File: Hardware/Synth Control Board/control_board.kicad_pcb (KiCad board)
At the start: 2 copper layers, 149.9 x 147.3 mm, 55 parts, among them J1 Conn_01x13, J10 Conn_01x05, J11 Conn_01x08, J2 Conn_01x03, J3 Conn_01x13, J4 Conn_01x13, J5 Conn_01x08, J6 Conn_01x13, J7 Conn_01x05, J8 Conn_01x05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

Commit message: redo control board layout. Initial version, might need more work.
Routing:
- net +5V: track 0.00 -> 1180.4 mm
- net /osc3_freq_wiper: track 0.00 -> 143.7 mm
- net /osc2_freq_wiper: track 0.00 -> 137.7 mm
- net /osc4_freq_wiper: track 0.00 -> 134.1 mm
- net /osc1_freq_wiper: track 0.00 -> 130.1 mm
- net /osc3_pwm_wiper: track 0.00 -> 123.3 mm
- net /osc4_pwm_wiper: track 0.00 -> 113.1 mm
- net /osc1_pwm_wiper: track 0.00 -> 112.9 mm
- net /osc2_pwm_wiper: track 0.00 -> 110.3 mm
- net /vol_out_1: track 0.00 -> 94.3 mm
- net /vol_in_1: track 0.00 -> 91.7 mm
- net /delay_out_1: track 0.00 -> 77.4 mm
- net /delay_in_1: track 0.00 -> 72.0 mm
- net /delay_out_2: track 0.00 -> 60.7 mm
- net /vol_out_4: track 0.00 -> 57.5 mm
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- added copper zone on B.Cu, net GND
- added copper zone on F.Cu, net GND

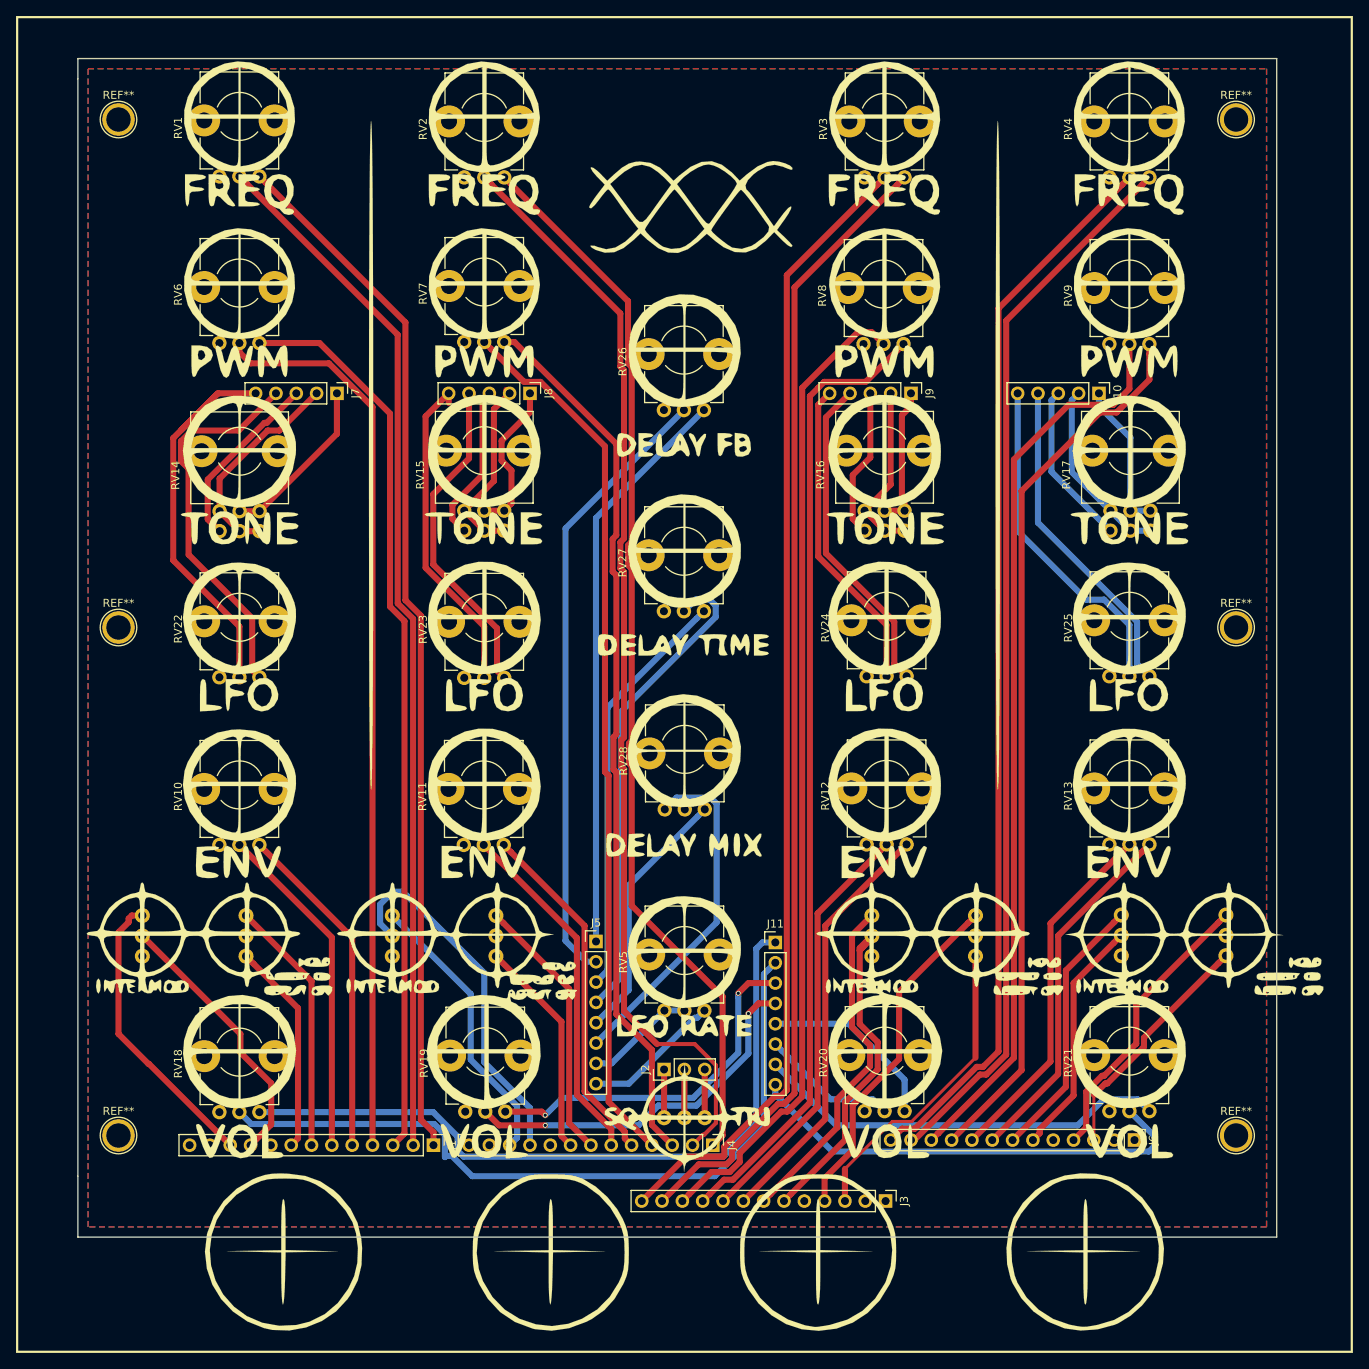
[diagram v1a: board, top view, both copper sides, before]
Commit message: add quantization again, fix connectors again, add mounting holes to main board
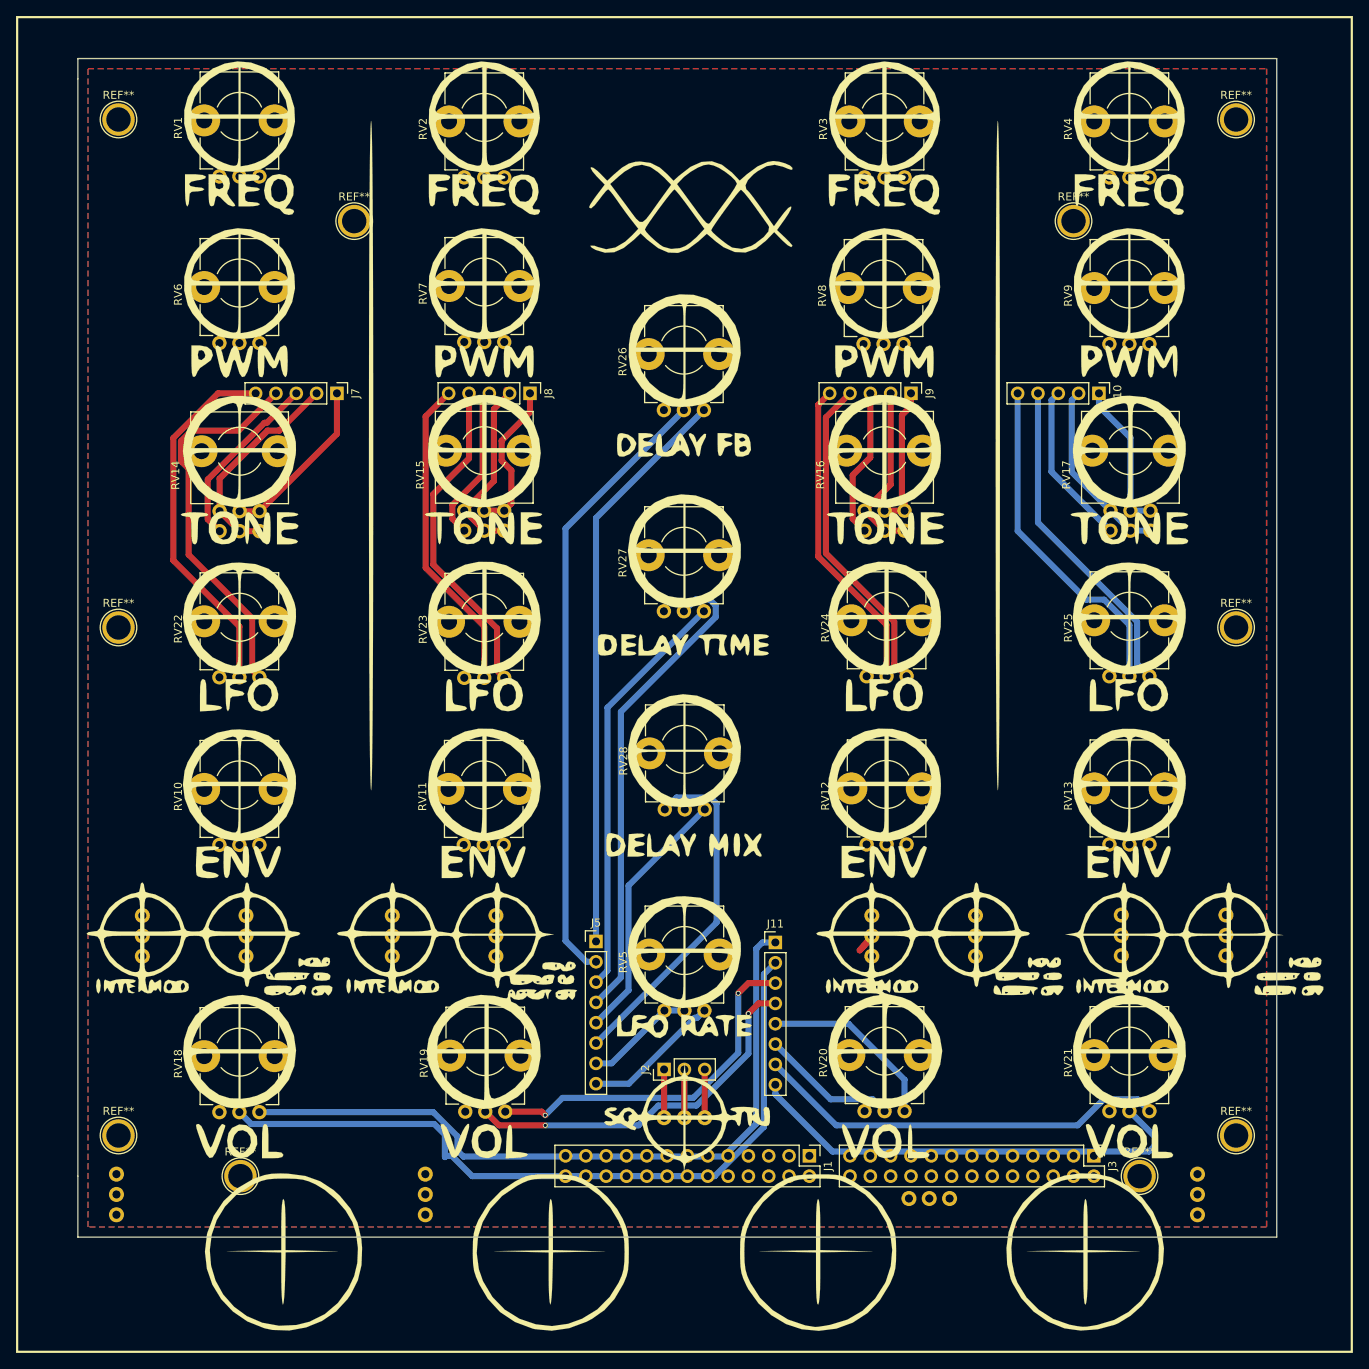
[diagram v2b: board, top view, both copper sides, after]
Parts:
- removed J4, J6: Conn_01x13, Pin_Headers:Pin_Header_Straight_1x13_Pitch2.54mm
- added REF**: 1pin, Connectors:1pin, F.Cu at (42.2, 25.4)
- added REF**: 1pin, Connectors:1pin, F.Cu at (132.1, 25.4)
- added REF**: 1pin, Connectors:1pin, F.Cu at (140.3, 144.8)
- added REF**: 1pin, Connectors:1pin, F.Cu at (27.9, 144.8)
- added SW10: SW_SPST, SparkFun-Electromechanical:SWITCH-SPDT, F.Cu at (28.6, 114.7)
- added SW11: SW_SPST, SparkFun-Electromechanical:SWITCH-SPDT, F.Cu at (59.9, 114.7)
- added SW12: SW_SPST, SparkFun-Electromechanical:SWITCH-SPDT, F.Cu at (119.8, 114.7)
- added SW13: SW_SPST, SparkFun-Electromechanical:SWITCH-SPDT, F.Cu at (151.1, 114.7)
- J1, J3: value Conn_01x13 -> Conn_02x13_Odd_Even; footprint Pin_Headers:Pin_Header_Straight_1x13_Pitch2.54mm -> Pin_Headers:Pin_Header_Straight_2x13_Pitch2.54mm
- moved J1 47.0 mm to (99.1, 142.2)
- moved SW9 36.2 mm to (12.4, 147.1)
- moved SW8 33.5 mm to (51.1, 147.1)
- moved SW7 33.3 mm to (114.0, 147.6), turned to 90 degrees
- moved SW6 32.6 mm to (147.6, 147.1)
- moved J3 26.6 mm to (134.6, 142.2)
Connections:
- J1 pad 10: /envelope_pwm_bypass_out_1 -> +5V
- J1 pad 11: /envelope_pwm_bypass_in_1 -> /osc1_speed
- J1 pad 12: GND -> /osc2_speed
- J1 pad 13: GND -> /osc1_hold
- J1 pad 2: /osc1_freq_wiper -> +5V
- J1 pad 3: +5V -> /osc1_freq_wiper
- J1 pad 4: /osc1_pwm_wiper -> /osc2_freq_wiper
- J1 pad 6: /osc1_speed -> +5V
- J1 pad 7: /osc1_hold -> /osc1_pwm_wiper
- J1 pad 8: /osc1_repeat -> /osc2_pwm_wiper
- J1 pad 9: /osc1_quant -> +5V
- J3 pad 10: +5V -> /osc4_quant
- J3 pad 11: /osc3_pwm_wiper -> /envelope_pwm_bypass_out_3
- J3 pad 12: +5V -> /envelope_pwm_bypass_out_4
- J3 pad 13: /osc3_freq_wiper -> /envelope_pwm_bypass_in_3
- J3 pad 3: /osc3_repeat -> GND
- J3 pad 4: /osc3_hold -> GND
- J3 pad 5: /osc3_quant -> /osc3_repeat
- J3 pad 6: /envelope_pwm_bypass_out_3 -> /osc4_repeat
- J3 pad 7: /envelope_pwm_bypass_in_3 -> /osc3_hold
- J3 pad 8: +5V -> /osc4_hold
- J3 pad 9: /osc3_speed -> /osc3_quant
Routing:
- net +5V: track 1180.4 -> 0.00 mm
- net /osc3_freq_wiper: track 143.7 -> 0.00 mm
- net /osc2_freq_wiper: track 137.7 -> 0.00 mm
- net /osc4_freq_wiper: track 134.1 -> 0.00 mm
- net /osc1_freq_wiper: track 130.1 -> 0.00 mm
- net /osc3_pwm_wiper: track 123.3 -> 0.00 mm
- net /osc4_pwm_wiper: track 113.1 -> 0.00 mm
- net /osc1_pwm_wiper: track 112.9 -> 0.00 mm
- net /osc2_pwm_wiper: track 110.3 -> 0.00 mm
- net /osc3_speed: track 53.0 -> 0.00 mm
- net /envelope_pwm_bypass_out_2: track 46.3 -> 0.00 mm
- net /osc4_speed: track 45.1 -> 0.00 mm
- net /osc2_speed: track 44.1 -> 0.00 mm
- net /osc3_hold: track 43.5 -> 0.00 mm
- net /envelope_pwm_bypass_in_3: track 43.2 -> 0.00 mm
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
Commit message: reroute connector board with 2-row connectors. Hold switch placement is temporary. Need to find room for this.
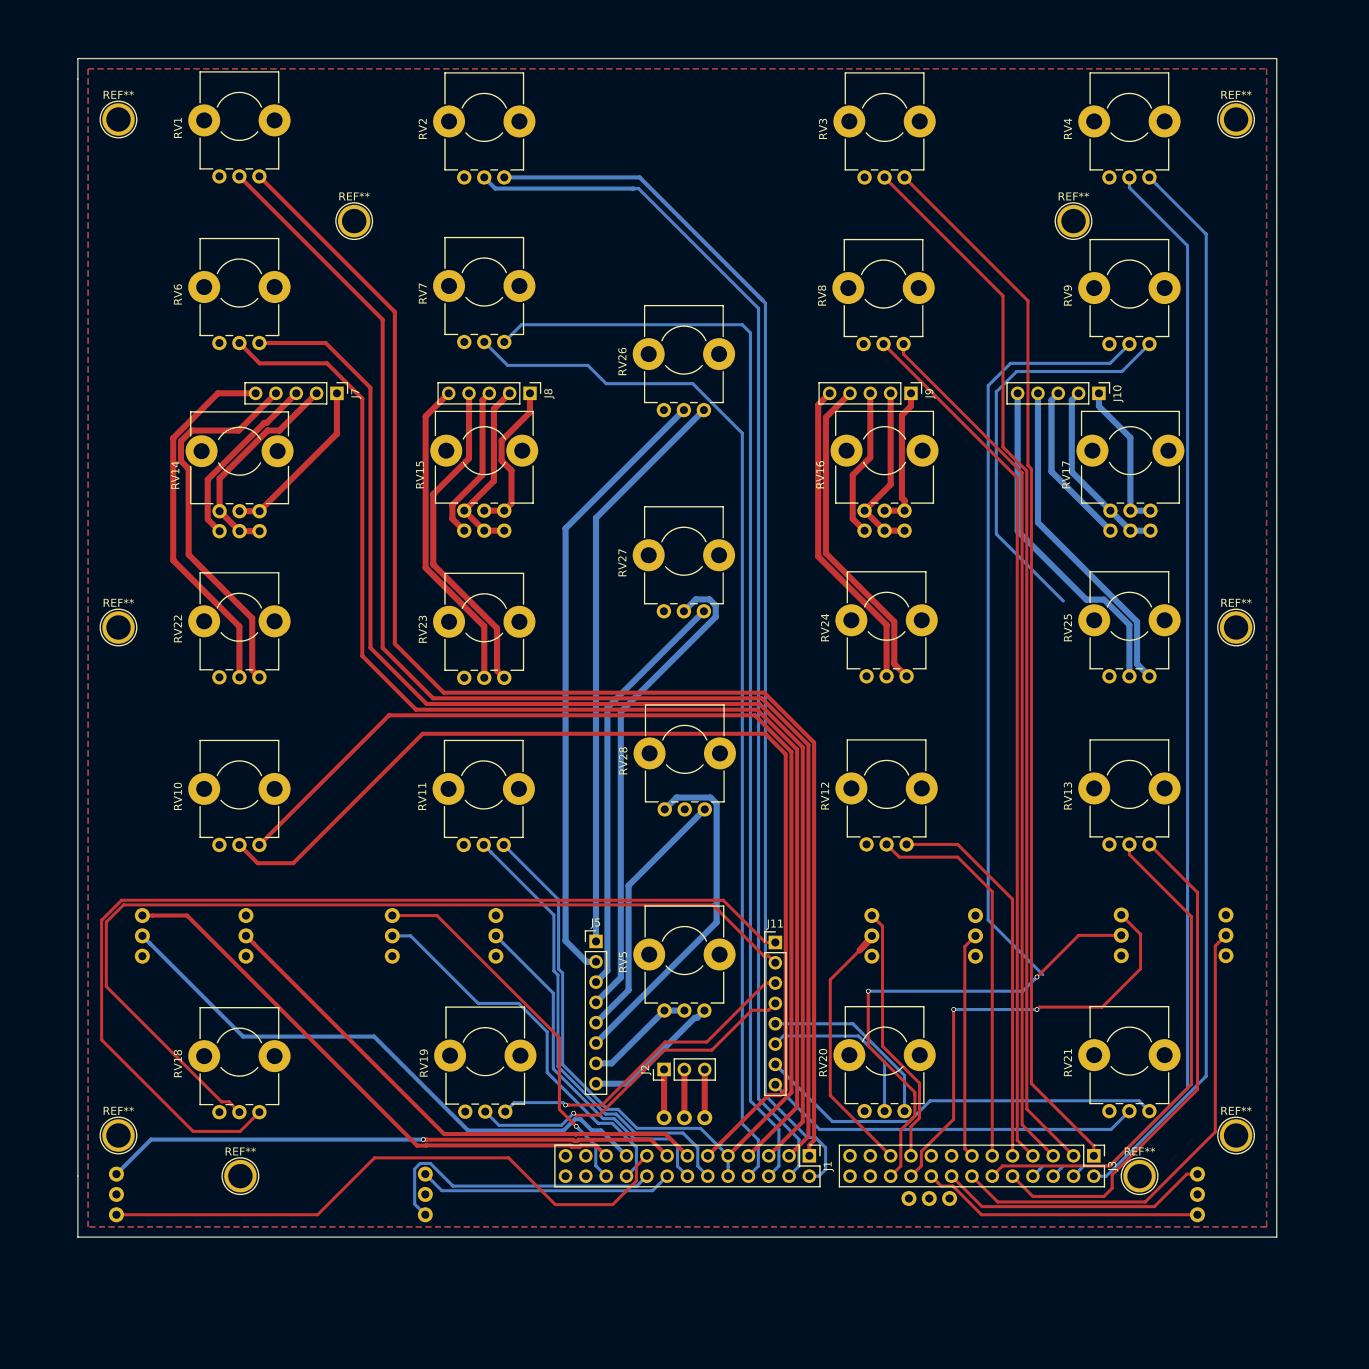
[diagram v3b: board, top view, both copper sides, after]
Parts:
- G***: moved to B.Cu
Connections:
- J1 pad 13: /osc1_hold -> /osc1_quant
- J1 pad 14: /osc2_hold -> /osc2_quant
- J1 pad 15: /osc1_repeat -> /osc1_hold
- J1 pad 16: /osc2_repeat -> /osc2_hold
- J1 pad 17: /osc1_quant -> /osc1_repeat
- J1 pad 18: /osc2_quant -> /osc2_repeat
- J3 pad 1: GND -> +5V
- J3 pad 10: /osc4_quant -> +5V
- J3 pad 11: /envelope_pwm_bypass_out_3 -> /osc3_speed
- J3 pad 12: /envelope_pwm_bypass_out_4 -> /osc4_speed
- J3 pad 13: /envelope_pwm_bypass_in_3 -> /osc3_quant
- J3 pad 14: /envelope_pwm_bypass_in_4 -> /osc4_quant
- J3 pad 15: +5V -> /osc3_hold
- J3 pad 16: +5V -> /osc4_hold
- J3 pad 17: /osc3_speed -> /osc3_repeat
- J3 pad 18: /osc4_speed -> /osc4_repeat
- J3 pad 19: +5V -> /envelope_pwm_bypass_in_3
- J3 pad 2: GND -> +5V
- J3 pad 20: +5V -> /envelope_pwm_bypass_in_4
- J3 pad 21: /osc3_pwm_wiper -> /envelope_pwm_bypass_out_3
- J3 pad 22: /osc4_pwm_wiper -> /envelope_pwm_bypass_out_4
- J3 pad 23: +5V -> GND
- J3 pad 24: +5V -> GND
- J3 pad 25: /osc3_freq_wiper -> GND
- J3 pad 26: /osc4_freq_wiper -> GND
- J3 pad 3: GND -> /osc3_freq_wiper
- J3 pad 4: GND -> /osc4_freq_wiper
- J3 pad 5: /osc3_repeat -> +5V
- J3 pad 6: /osc4_repeat -> +5V
- J3 pad 7: /osc3_hold -> /osc3_pwm_wiper
- J3 pad 8: /osc4_hold -> /osc4_pwm_wiper
- J3 pad 9: /osc3_quant -> +5V
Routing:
- net +5V: track 0.00 -> 1356.8 mm
- net /osc1_freq_wiper: track 0.00 -> 177.0 mm
- net /osc1_pwm_wiper: track 0.00 -> 162.9 mm
- net /osc2_freq_wiper: track 0.00 -> 152.4 mm
- net /osc4_freq_wiper: track 0.00 -> 135.7 mm
- net /osc1_speed: track 0.00 -> 132.1 mm
- net /osc3_freq_wiper: track 0.00 -> 132.1 mm
- net /osc2_pwm_wiper: track 0.00 -> 131.2 mm
- net /osc3_pwm_wiper: track 0.00 -> 109.2 mm
- net /osc4_pwm_wiper: track 0.00 -> 98.0 mm
- net /osc1_repeat: track 0.00 -> 75.3 mm
- net /envelope_pwm_bypass_out_1: track 0.00 -> 73.1 mm
- net /osc1_hold: track 0.00 -> 71.6 mm, vias 0 -> 1
- net /envelope_pwm_bypass_in_1: track 0.00 -> 70.6 mm
- net /osc1_quant: track 0.00 -> 66.6 mm
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
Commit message: increase control board size to accomodate hold switch placement. Hopefully, this is the final panel design.
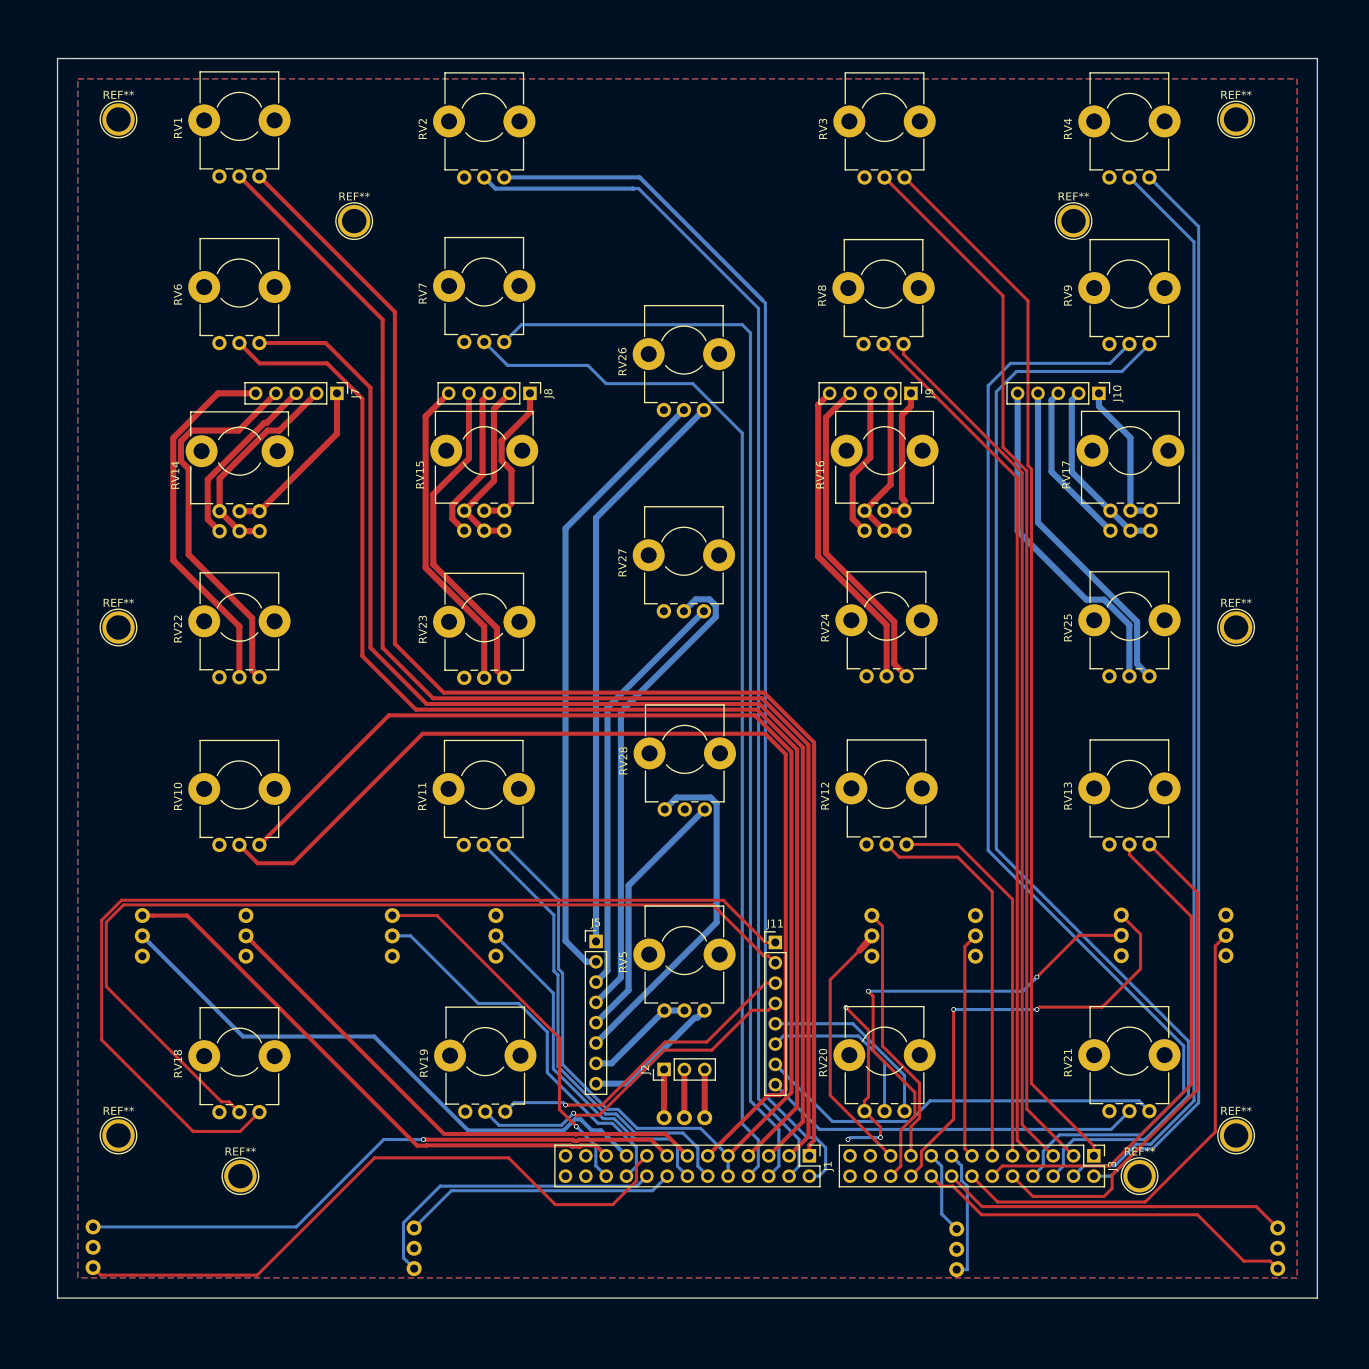
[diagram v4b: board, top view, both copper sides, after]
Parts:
- removed G***: LOGO, Panel Artwork:panel_silkscreen
- moved SW6 12.1 mm to (157.6, 153.8)
- moved SW9 7.22 mm to (9.53, 153.7)
- moved SW7 7.22 mm to (117.5, 153.9), turned to 180 degrees
- moved SW8 6.87 mm to (49.7, 153.8)
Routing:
- net +5V: track 1356.8 -> 1446.2 mm
- net /osc4_pwm_wiper: track 98.0 -> 142.5 mm
- net GND: track 0.00 -> 22.6 mm, vias 0 -> 3
- net /osc3_hold: track 0.00 -> 16.4 mm
- net /osc4_repeat: track 35.3 -> 48.1 mm
- net /osc3_repeat: track 0.00 -> 10.5 mm
- net /osc4_hold: track 34.0 -> 43.9 mm
- net /osc1_repeat: track 75.3 -> 81.7 mm
- net /osc1_hold: track 71.6 -> 77.3 mm
- net /osc2_hold: track 31.8 -> 34.3 mm
- net /osc4_freq_wiper: track 135.7 -> 137.7 mm
- net /osc2_repeat: track 37.3 -> 39.1 mm
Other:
- board size 149.9 x 147.3 mm -> 157.5 x 154.9 mm
